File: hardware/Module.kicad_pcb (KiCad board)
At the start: 2 copper layers, 47.6 x 109.2 mm, 123 parts, among them J1 Jack, J10 Jack, J11 Jack, J12 Jack, J13 Micro_SD, J14 Jack, J15 Jack, J16 Jack, J17 Power, J18 Jack, J19 Jack, J2 OLED, J4 Jack, J5 Jack, J6 Jack, J7 Jack, J8 Jack, J9 Jack, SW1 Encoder, SW2 Encoder, U1 TL074, U2 TL074, U3 TL074, U4 MCP6004, U5 MCP6002, U6 TLP2361, U7 LM4040C10

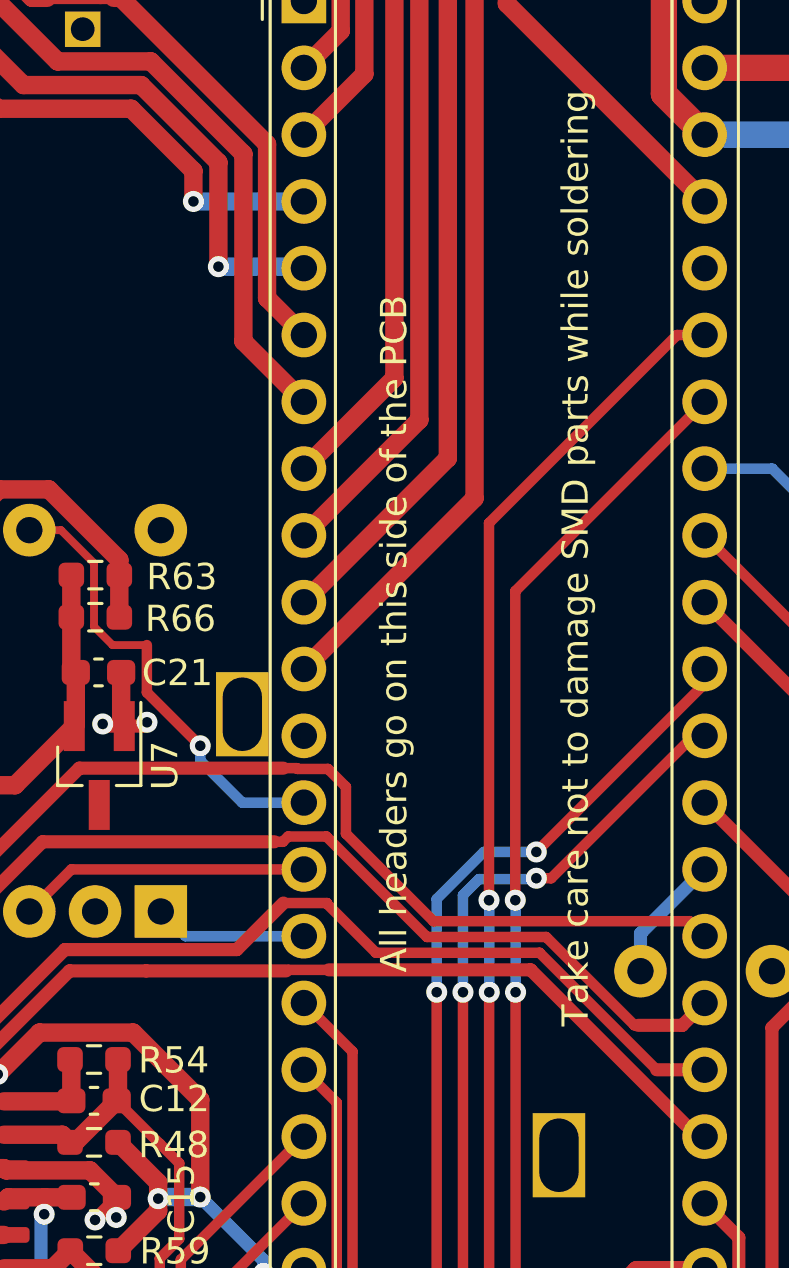
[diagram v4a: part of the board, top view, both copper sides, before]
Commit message: Remove misleading label
Signed-off-by: Petr Horacek <hrck@protonmail.com>
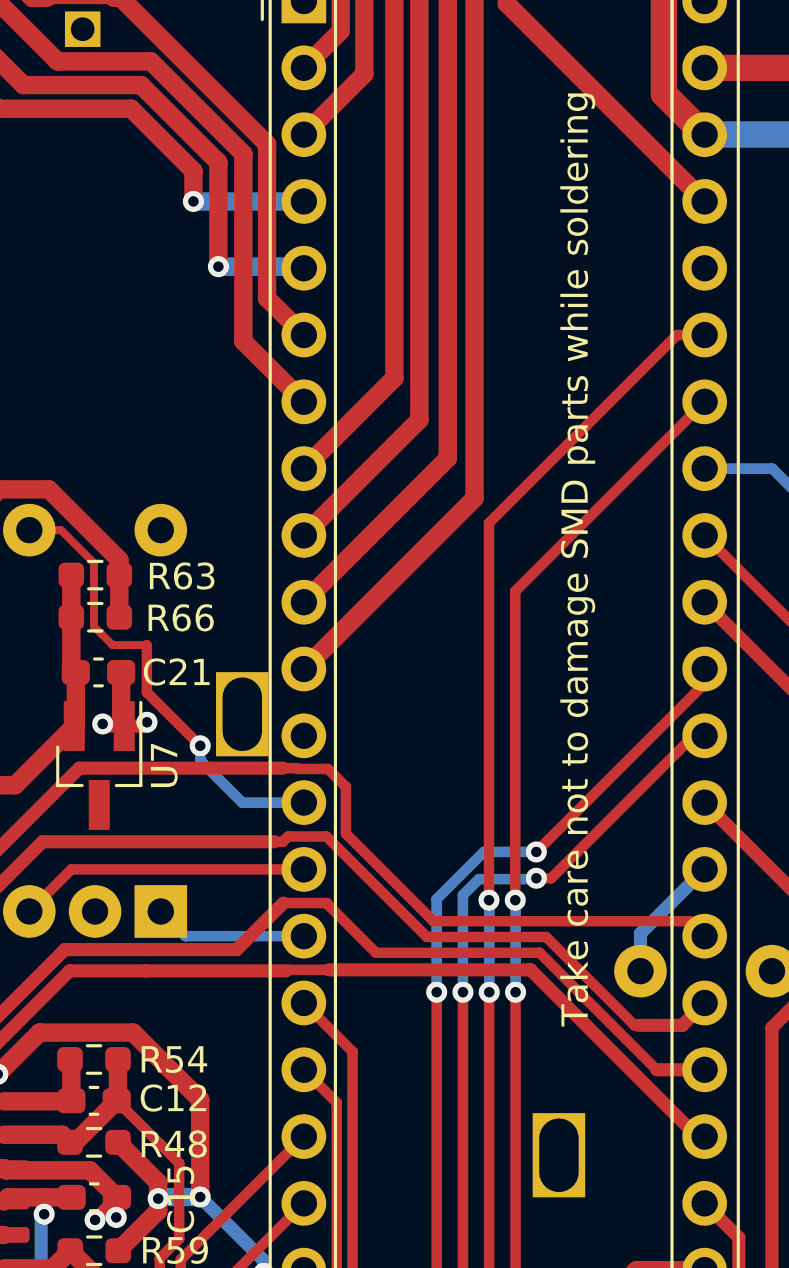
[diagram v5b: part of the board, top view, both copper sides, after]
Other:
- board text removed: "All headers go on this side of the PCB"

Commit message: Update to KiCad 6
Signed-off-by: Petr Horacek <hrck@protonmail.com>
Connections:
- A1 pad 1: Net-(A1-Pad1) -> unconnected-(A1-Pad1)
- A1 pad 12: Net-(A1-Pad12) -> unconnected-(A1-Pad12)
- A1 pad 36: Net-(A1-Pad36) -> unconnected-(A1-Pad36)
- FB1 pad 1: Net-(D3-Pad2) -> Net-(J17-Pad10)
- FB1 pad 2: Net-(FB1-Pad2) -> Net-(D3-Pad2)
- FB2 pad 1: Net-(D4-Pad1) -> Net-(J17-Pad1)
- FB2 pad 2: Net-(FB2-Pad2) -> Net-(D4-Pad1)
- J10 pad TN: Net-(J10-PadTN) -> unconnected-(J10-PadTN)
- J11 pad TN: Net-(J11-PadTN) -> unconnected-(J11-PadTN)
- J12 pad TN: Net-(J12-PadTN) -> unconnected-(J12-PadTN)
- J17 pad 1: Net-(FB2-Pad2) -> Net-(J17-Pad1)
- J17 pad 10: Net-(FB1-Pad2) -> Net-(J17-Pad10)
- J17 pad 2: Net-(FB2-Pad2) -> Net-(J17-Pad1)
- J17 pad 9: Net-(FB1-Pad2) -> Net-(J17-Pad10)
- J7 pad TN: Net-(J7-PadTN) -> unconnected-(J7-PadTN)
- J8 pad TN: Net-(J8-PadTN) -> unconnected-(J8-PadTN)
- J9 pad TN: Net-(J9-PadTN) -> unconnected-(J9-PadTN)
- U5 pad 5: Net-(U5-Pad5) -> unconnected-(U5-Pad5)
- U5 pad 6: Net-(U5-Pad6) -> unconnected-(U5-Pad6)
- U5 pad 7: Net-(U5-Pad7) -> unconnected-(U5-Pad7)
- U6 pad 2: Net-(U6-Pad2) -> unconnected-(U6-Pad2)
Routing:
- net Net-(J17-Pad10): track 0.00 -> 26.8 mm
- net Net-(FB1-Pad2): track 26.8 -> 0.00 mm
- net Net-(J17-Pad1): track 0.00 -> 21.1 mm
- net Net-(FB2-Pad2): track 21.1 -> 0.00 mm
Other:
- net class Default removed

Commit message: Release version 0.2.0
Signed-off-by: Petr Horacek <hrck@protonmail.com>
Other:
- board text added: "board v0.2.0"
- board text removed: "board v0.1.0"
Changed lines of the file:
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@@
     (title "Proton")
     (date "2022-03-06")
-    (rev "v0.1.0")
+    (rev "v0.2.0")
     (company "Petr Horáček")
     (comment 1 "petr@zlosynth.com")
@@
     (effects (font (size 1 1) (thickness 0.15)))
   )
-  (gr_text "board v0.1.0" (at 158.77 58.98 90) (layer "F.SilkS")
+  (gr_text "board v0.2.0" (at 158.77 58.98 90) (layer "F.SilkS")
     (effects (font (size 1 1) (thickness 0.15)) (justify left))
   )

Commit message: Release version 0.3.0
Signed-off-by: Petr Horacek <hrck@protonmail.com>
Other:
- board text added: "board v0.3.0"
- board text removed: "board v0.2.0"
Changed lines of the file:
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@@
     (title "Proton")
     (date "2022-03-06")
-    (rev "v0.2.0")
+    (rev "v0.3.0")
     (company "Petr Horáček")
     (comment 1 "petr@zlosynth.com")
@@
     (effects (font (size 1 1) (thickness 0.15)))
   )
-  (gr_text "board v0.2.0" (at 158.77 58.98 90) (layer "F.SilkS")
+  (gr_text "board v0.3.0" (at 158.77 58.98 90) (layer "F.SilkS")
     (effects (font (size 1 1) (thickness 0.15)) (justify left))
   )
